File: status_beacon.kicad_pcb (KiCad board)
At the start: 2 copper layers, 65 x 64.5 mm, 59 parts, among them J1 USB_C_16P, J2 SWD_TC2030, SW1 K2-1187SQ-A4SW-06, U1 PY32F003F18P6TU

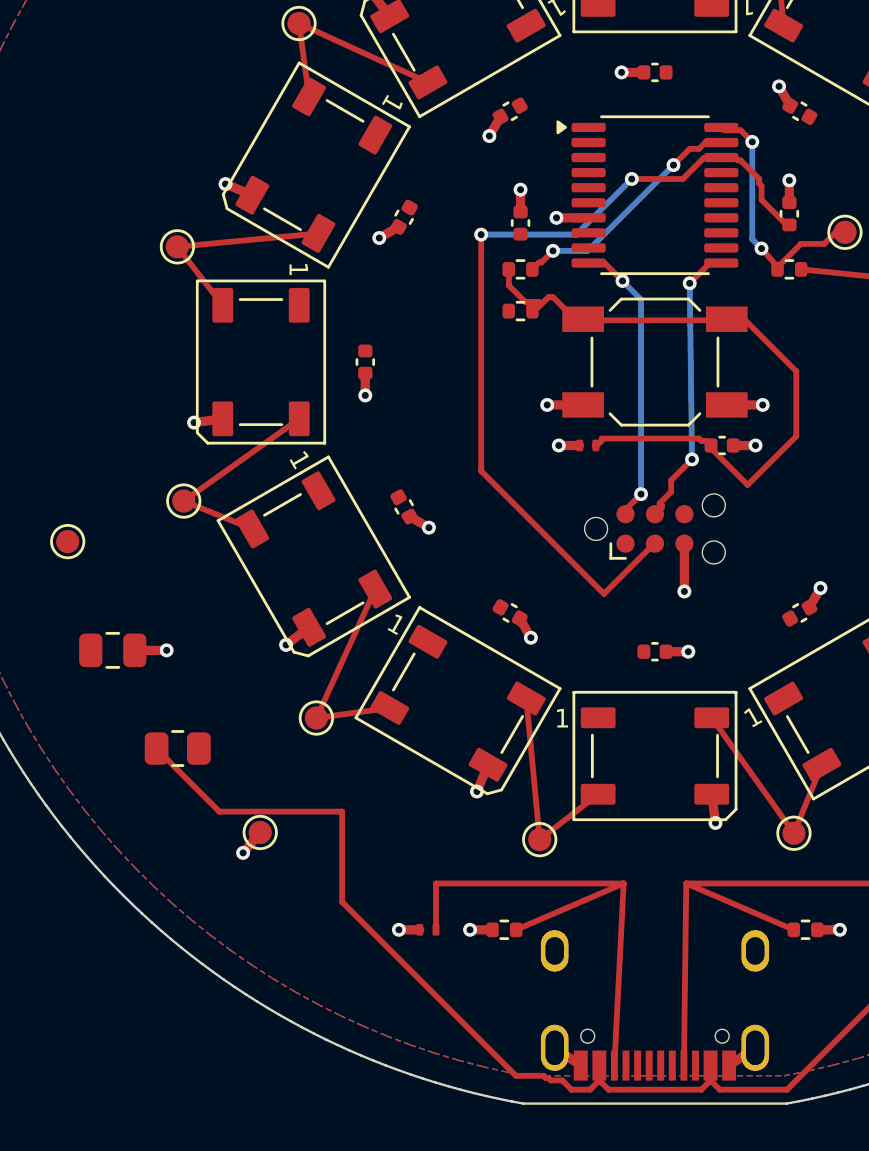
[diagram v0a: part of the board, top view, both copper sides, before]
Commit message: Series Schottky, and move off the discontinued LED
R3 (0R) becomes D17, a 1N5819WS Schottky in the VBUS to +5V path: a JLCPCB
basic part at $0.0116 with 1 A rating and Vf <= 0.60 V at 1 A. D1-D12 move
from WS2812B-B/T, which JLCPCB flags discontinued, to WS2812B-V5/W. The MCU
is unchanged: PY32F003F18P6TU is already the x6 variant, 1.7-5.5 V, so it
spans the whole post-diode rail with 2.65 V to spare below it.

The declared rails are now what the parts and the source actually permit.
VBUS is 4.75-5.5 V, which is vSafe5V rather than a narrower claim, so
usb_source_range_coverage passes on the truth instead of failing on a
declaration that did not cover the source. +5V runs from 4.15 V - the source
minimum less the diode's maximum forward voltage - up to 5.5 V, because no
diode datasheet guarantees a MINIMUM forward voltage and so nothing bounds
the rail from above.

That is the whole trade, and the claim model now states it exactly: the LED
absolute-maximum margins read -0.2 V as a LOWER bound, so their verdicts are
UNKNOWN rather than FAIL. The evidence cannot prove the rail exceeds 5.3 V
and cannot prove it does not. Rules go from 1 FAIL / 34 PASS / 11 UNKNOWN to
0 FAIL / 23 PASS / 23 UNKNOWN.

The V5 datasheet is better than the one it replaces and supersedes three
numbers. Working current is 12 mA per channel, so 36 mA per LED where 60 mA
had been assumed, taking the ring from 0.468 A to 0.281 A on direct evidence.
The shortest data high time is 220 ns, not 400 ns. VIH eases to 0.63xVDD
while VIL tightens to an absolute 0.7 V, and there is no characterised supply
range at all, only a 5 V test point - so the droop scenario now asserts
against the 3.7 V absolute minimum, driven at the source minimum less the
diode's maximum drop, which makes its 4.104 V result a lower bound.

Two rules were too narrow to survive the swap and are generalised rather than
patched: probe_access looked for an R-prefixed supply link when what it means
is exactly one two-terminal element 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
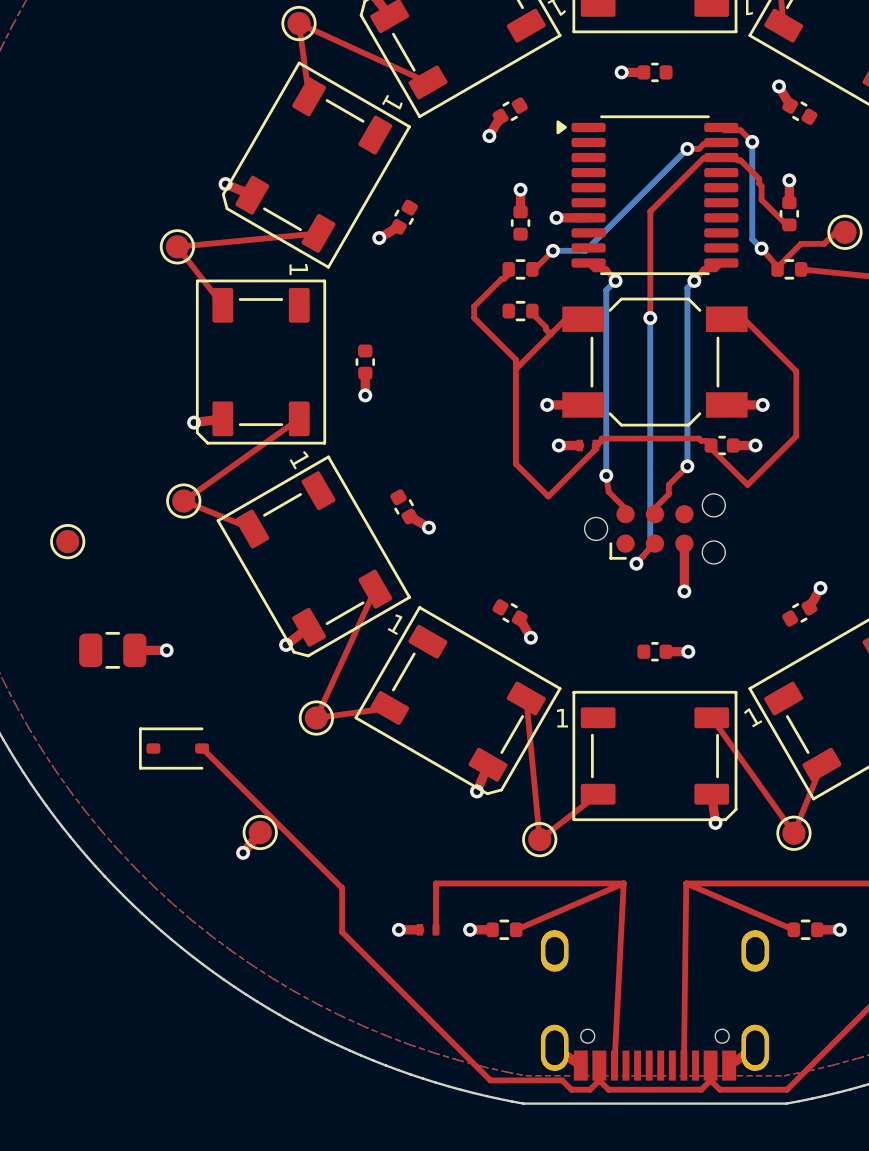
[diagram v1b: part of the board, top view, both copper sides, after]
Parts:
- removed R3: 0R, Resistor_SMD:R_0805_2012Metric
- added D17: 1N5819WS, Diode_SMD:D_SOD-323, F.Cu at (79.4, 116.7)
- D1, D10, D11, D12, D2, D3, D4, D5, D6, D7, D8, D9: value WS2812B-B/T -> WS2812B-V5/W
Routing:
- net NRST: track 37.2 -> 25.3 mm
- net BTN_SW: track 29.0 -> 37.4 mm
- net VBUS: track 62.4 -> 59.2 mm

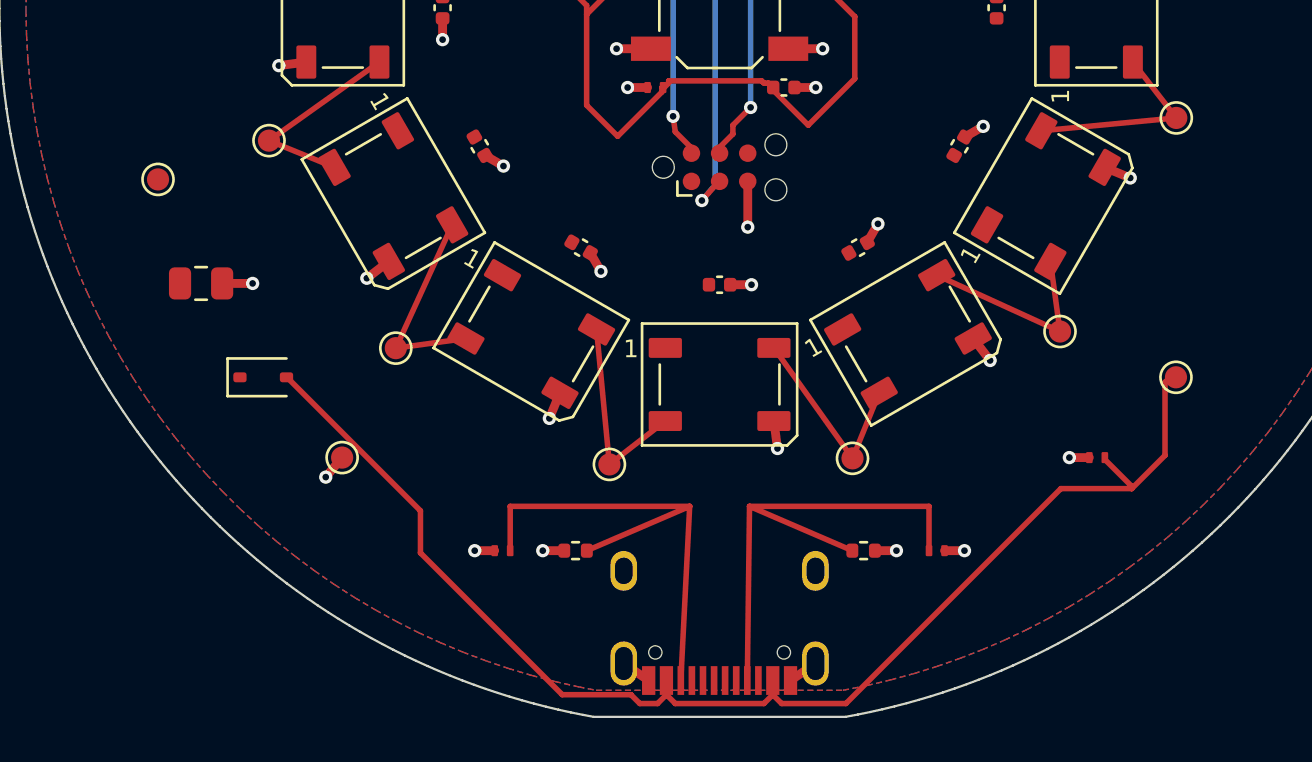
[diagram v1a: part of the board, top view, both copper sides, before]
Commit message: Regulate the rail: ME6211C50 LDO replaces the series Schottky
D17 and its 2 mV of margin are gone. U2 is an ME6211C50M5G-N in SOT-23-5,
with C17 as its input capacitor on VBUS; C1 stays on the output. The rail is
now the regulator's specified band rather than a source minus a drop nobody
guarantees: 4.05 to 5.05 V, against the WS2812B-V5's 3.70 to 5.30 V absolute
range. High margin +250 mV comes off the datasheet's +/-1% output tolerance;
low margin +350 mV from its dropout extrapolated to the declared port budget
and derated for temperature.

That is the whole point of the change. The twelve LED absolute-maximum checks
no longer report UNKNOWN because a lower bound could not decide them; they
PASS on a specified number. Board rules go from 0 FAIL / 23 PASS / 23 UNKNOWN
to 0 FAIL / 36 PASS / 11 UNKNOWN, and the eleven that remain are the
WS2812B's unspecified DOUT levels, which no part choice can settle.

Three things the regulator broke, each fixed by deriving from the topology
rather than restating it. The +5V power flag became a second power-output pin
once VOUT actually drove the net, so it is gone and VBUS and GND keep theirs.
The inrush rule summed capacitance across a hardcoded VBUS-plus-5V domain,
which was right when a link joined them and wrong once a regulator separated
them; it now walks the nets reachable through series passives, so only C17
counts. The supply-link rule required a two-terminal bridge; it now accepts
any single part touching both rails.

The SOT-23-5 needs more of the service arc than the 0805 link it replaced,
so that group is re-spaced from 11 to 9 degrees and shifted to clear the
courtyard overlap the first attempt hit.

23 gates pass, 62 tests pass, $1.7356 per board at qty 50.

Co-Authored-By: Claude Opus 5 <noreply@anthropic.com>
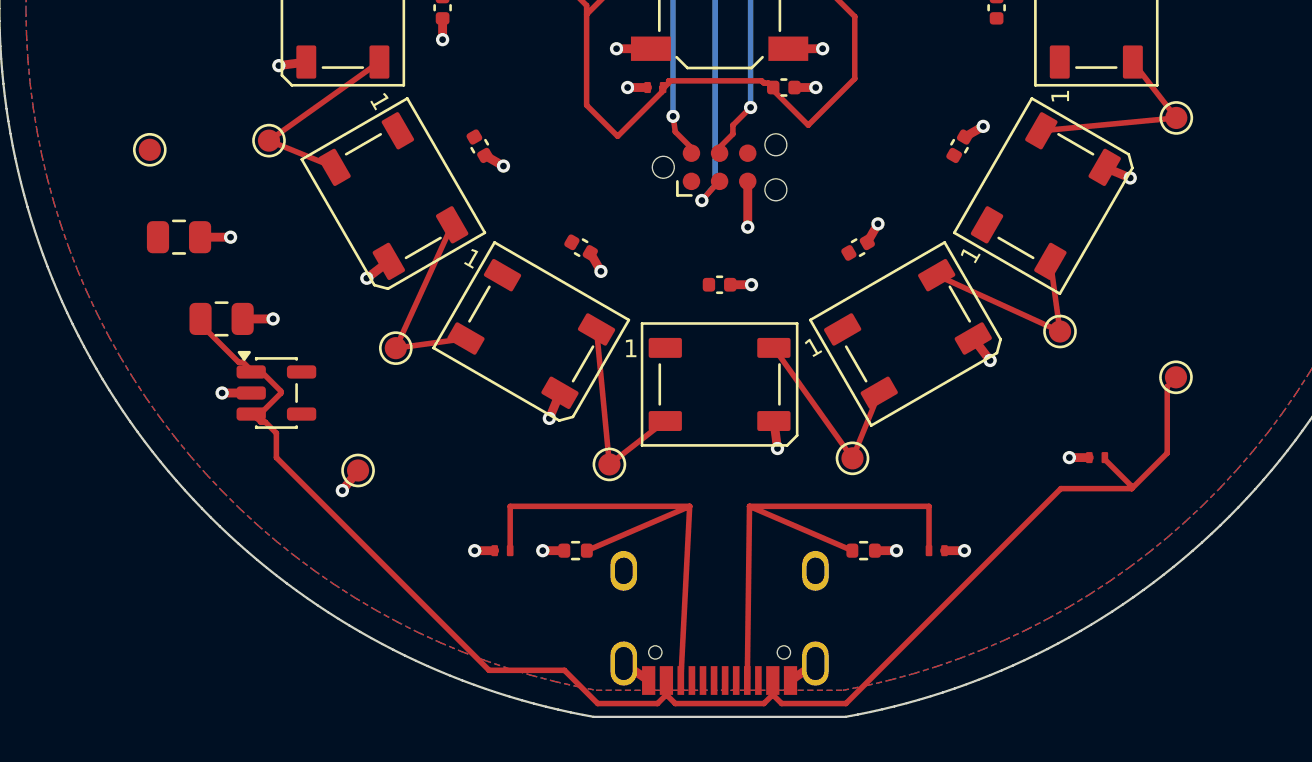
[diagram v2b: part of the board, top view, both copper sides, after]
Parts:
- removed D17: 1N5819WS, Diode_SMD:D_SOD-323
- added C17: 4.7uF, Capacitor_SMD:C_0805_2012Metric, F.Cu at (77.5, 114.0)
- added U2: ME6211C50M5G-N, Package_TO_SOT_SMD:SOT-23-5, F.Cu at (80.0, 117.4)
- moved C1 2.31 mm to (75.6, 110.4)
- moved TP2 1.39 mm to (74.3, 106.4)
- moved TP3 0.92 mm to (83.7, 120.9)
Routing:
- net VBUS: track 59.2 -> 66.5 mm
- net GND: track 46.7 -> 49.4 mm, vias 39 -> 41
